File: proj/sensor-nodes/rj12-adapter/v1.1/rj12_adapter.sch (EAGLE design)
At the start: 47 parts, among them J1 54602-908LF, J2 54602-908LF, J5 OPENAG-I2C-RJ12, J6 OPENAG-I2C-RJ12, U2 PCA9615, U3 MIC4680, U4 LM2937

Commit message: added rj12 adapter v1.1
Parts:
- removed C4: 15uF, openag-capacitors:15UF-C2012X5R1V156M125AC
- removed C5: 220uF, openag-capacitors:220UF-TPSY227K010R0100
- removed D4: SBR2A40P1-7, openag-diodes:SBR2A40P1-7
- removed D5: APT1608, openag-diodes:APT1608CGCK
- removed R5: 3.01K, openag-resistors:3.01K-RC0603FR-073K01L
- removed R6: 976 Ohm, openag-resistors:982OHM-RC0603FR-07976RL
- removed R7: 100, openag-resistors:100OHM-RC0603JR-07100RL
- removed SJ2: (no value), openag-connectors:SOLDERJUMPERREFLOW_NOPASTE
- removed TP5, TP6, TP7: TPTP06R, openag-testpads:TPTP06R
- removed U3: MIC4680, openag-regulators:MIC4680YM-TR
- added C1, C2, C3: 10uF, openag-capacitors:10UF-GMK212BBJ106KG-T
- added D2: APT1608, openag-diodes:APT1608CGCK
- added R1: 100, openag-resistors:100OHM-RC0603JR-07100RL
- added TP1, TP2, TP3: TPTP06R, openag-testpads:TPTP06R
- added U1: R-78E5.0-1.0, openag-regulators:R-78E5.0-1.0
- FRAME1: VER (none) -> 1.1
- L1: value 68uH -> 33uH; device openag-inductors:68UH-UP2B-680-R -> openag-inductors:33UH-29333C
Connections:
- removed net N$31: D4.12, L1.1, R5.1, R6.2, U3.FB, U3.SW
- removed net N$32: D5.A, R7.1
- removed net N$33: C5.1(+), L1.2, R5.2, R7.2, SJ2.1
- new net 24V_EMI: C1.1, L1.2, U1.VIN
- new net N$6: D2.A, R1.1
- net +24V: now also C3.1, L1.1, TP1.TP; no longer C4.1, TP7.TP, U3.IN
- net +5V: now also C2.1, R1.2, TP3.TP, U1.VOUT; no longer SJ2.2, TP5.TP
- net GND: now also C1.2, C2.2, C3.2, D2.C, TP2.TP, U1.GND; no longer C4.2, C5.2(-), D4.21, D5.C, R6.1, TP6.TP, U3.GND, U3.SHDN
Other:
- note added: "8-28V to 5V@1A Switching Regulator w/Class B EMI Filter + Indicator LED"
- note added: "EMI Filter"
- note added: "Indicator LED"
- note added: "Switching Regulator"
- note removed: "24V to 5V@1A Switching Regulator w/Indicator LED + Enable"
- moved on the sheet: J5, J6, TP11, TP12, TP13, TP14, TP32, TP33, TP34, TP35, TP8, TP9

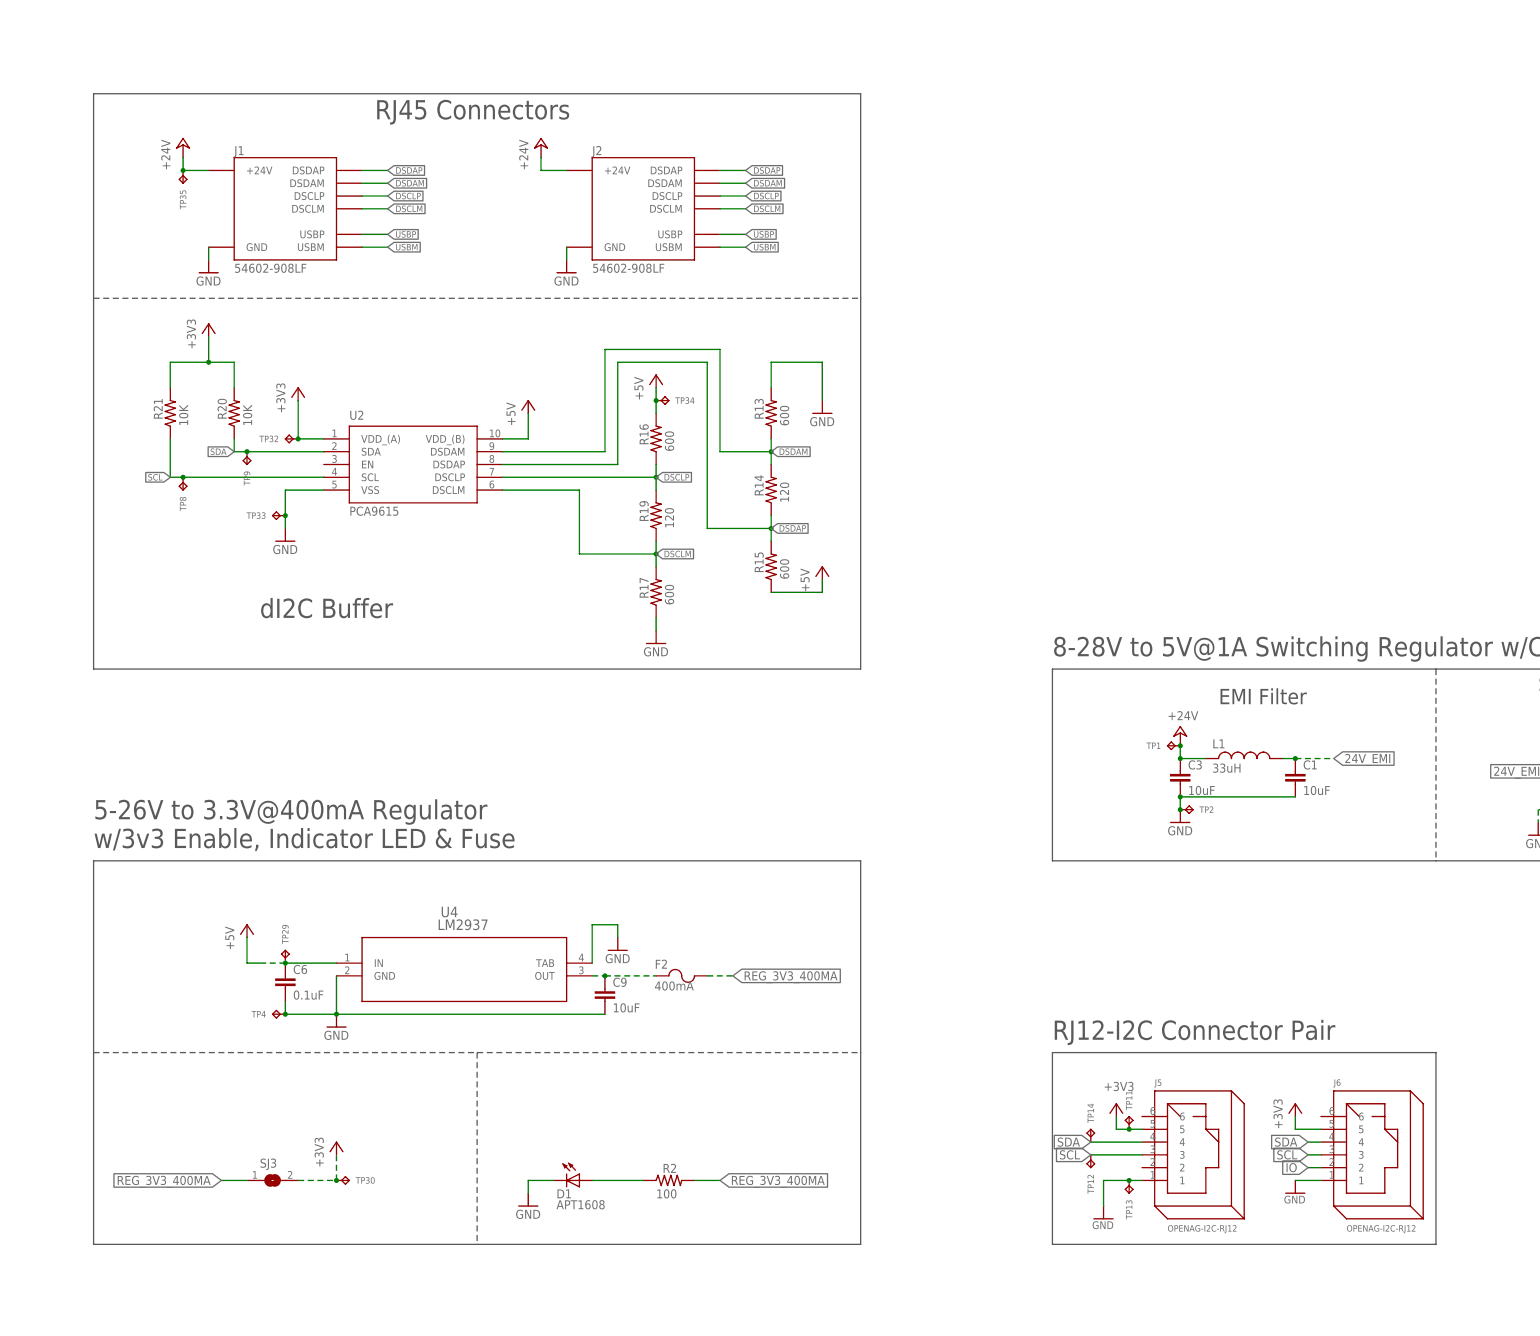
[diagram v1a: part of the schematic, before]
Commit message: cleaned up regulator design blocks
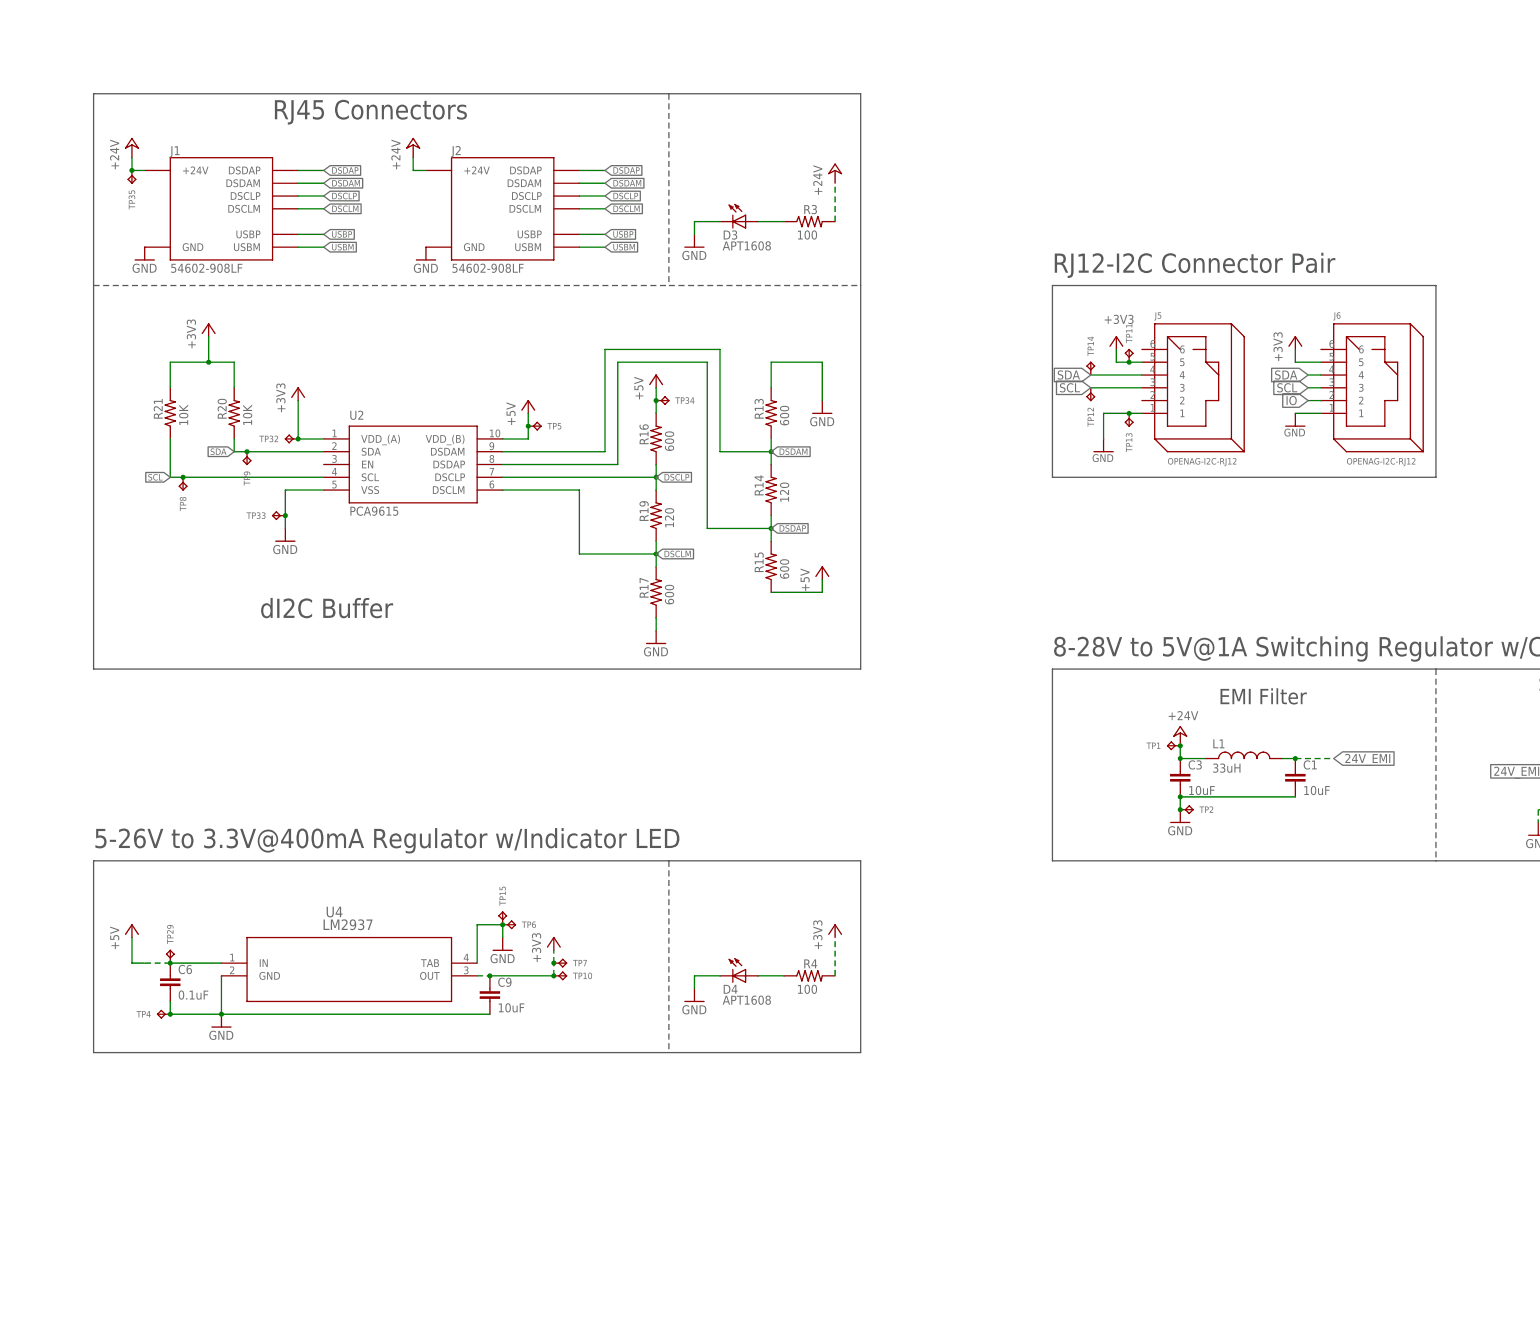
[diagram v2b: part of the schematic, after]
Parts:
- removed D1: APT1608, openag-diodes:APT1608CGCK
- removed F2: 400mA, openag-fuses:0438.375WR
- removed R2: 100, openag-resistors:100OHM-RC0603JR-07100RL
- removed SJ3: (no value), openag-connectors:SOLDERJUMPERREFLOW_NOPASTE
- removed TP30: TPTP06R, openag-testpads:TPTP06R
- added D3, D4: APT1608, openag-diodes:APT1608CGCK
- added R3, R4: 100, openag-resistors:100OHM-RC0603JR-07100RL
- added TP10, TP15, TP5, TP6, TP7: TPTP06R, openag-testpads:TPTP06R
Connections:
- removed net N$4: D1.A, R2.1
- removed net REG_3V3_400MA: F2.2, R2.2, SJ3.1
- new net N$7: D3.A, R3.1
- net +24V: now also R3.2
- net +3V3: now also C9.1, R4.2, TP10.TP, TP7.TP, U4.OUT; no longer SJ3.2, TP30.TP
- net +5V: now also TP5.TP
- net GND: now also D3.C, D4.C, TP15.TP, TP6.TP; no longer D1.C
- net N$5: now also D4.A, R4.1; no longer C9.1, F2.1, U4.OUT
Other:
- note added: "5-26V to 3.3V@400mA Regulator w/Indicator LED"
- note removed: "3.3V Enable Jumper"
- note removed: "3.3V Indicator LED"
- note removed: "5-26V to 3.3V@400mA Regulator w/3v3 Enable, Indicator LED & Fuse"
- moved on the sheet: C6, C9, J1, J2, J5, J6, TP11, TP12, TP13, TP14, TP29, TP35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

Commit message: improving keyboard shortcuts
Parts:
- removed J2: 54602-908LF, openag_connector:OPENAG-V1-RJ45PTH
- added J3: 54602-908LF, openag_connector:OPENAG-V1-RJ45PTH
- added R12, R22, R23, R24: 600, openag-resistors:600OHM-RC0603FR-07604RL
- added R18, R25: 120, openag-resistors:120OHM-RC0603FR-07120RL
- added U5: PCA9615, openag-buffers:PCA9615DPJ
- R3: value 100 -> 1K; device openag-resistors:100OHM-RC0603JR-07100RL -> openag-resistors:1K-ERJ-PB3D1001V
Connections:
- removed net DSCLM: J1.DSCLM, J2.DSCLM, R17.2, R19.1, U2.DSCLM
- removed net DSCLP: J1.DSCLP, J2.DSCLP, R16.1, R19.2, U2.DSCLP
- removed net DSDAM: J1.DSDAM, J2.DSDAM, R13.1, R14.2, U2.DSDAM
- removed net DSDAP: J1.DSDAP, J2.DSDAP, R14.1, R15.2, U2.DSDAP
- new net DSCLM_1: J1.DSCLM, R17.2, R19.1, U2.DSCLM
- new net DSCLM_2: J3.DSCLM, R24.2, R25.1, U5.DSCLM
- new net DSCLP_1: J1.DSCLP, R16.1, R19.2, U2.DSCLP
- new net DSCLP_2: J3.DSCLP, R23.1, R25.2, U5.DSCLP
- new net DSDAM_1: J1.DSDAM, R13.1, R14.2, U2.DSDAM
- new net DSDAM_2: J3.DSDAM, R12.1, R18.2, U5.DSDAM
- new net DSDAP_1: J1.DSDAP, R14.1, R15.2, U2.DSDAP
- new net DSDAP_3: J3.DSDAP, R18.1, R22.2, U5.DSDAP
- net +24V: now also J3.+24V; no longer J2.+24V
- net +3V3: now also U5.VDD_(A)
- net +5V: now also R22.1, R23.2, U5.VDD_(B)
- net GND: now also J3.GND, R12.2, R24.1, U5.VSS; no longer J2.GND
- net SCL: now also U5.SCL
- net SDA: now also U5.SDA
- net USBM: now also J3.USBM; no longer J2.USBM
- net USBP: now also J3.USBP; no longer J2.USBP
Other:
- note added: "RJ45 Connector Pair w/dI2C Buffer + Indicator LED"
- note added: "dI2C Buffer Channel 1"
- note added: "dI2C Buffer Channel 2"
- note removed: "RJ45 Connector w/dI2C Buffer"
- note removed: "dI2C Buffer"
- moved on the sheet: C1, C2, C3, C6, C9, D2, D3, D4, J1, J5, J6, L1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
